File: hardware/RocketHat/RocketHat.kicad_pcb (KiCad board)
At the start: 4 copper layers, 28 x 25 mm, 31 parts, among them J1 Conn_02x16_Top_Bottom, J2 Conn_02x16_Top_Bottom, Q2 MMBT2222A, SW1 SW_DIP_x01, U1 BMP390, U2 BMI088, U3 ADXL375BCCZ, U5 74HC688, U6 74HC245, U7 74HC245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

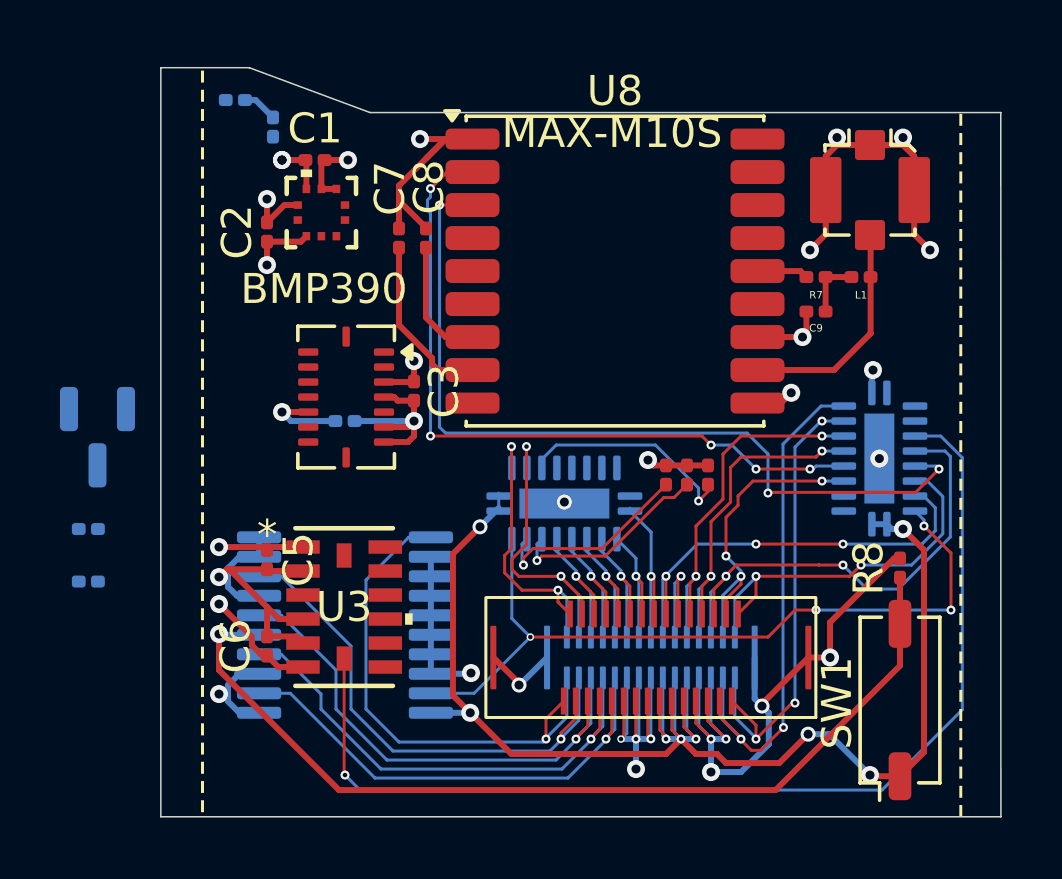
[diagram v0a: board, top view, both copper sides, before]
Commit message: rocket hat finished routing 4 layer
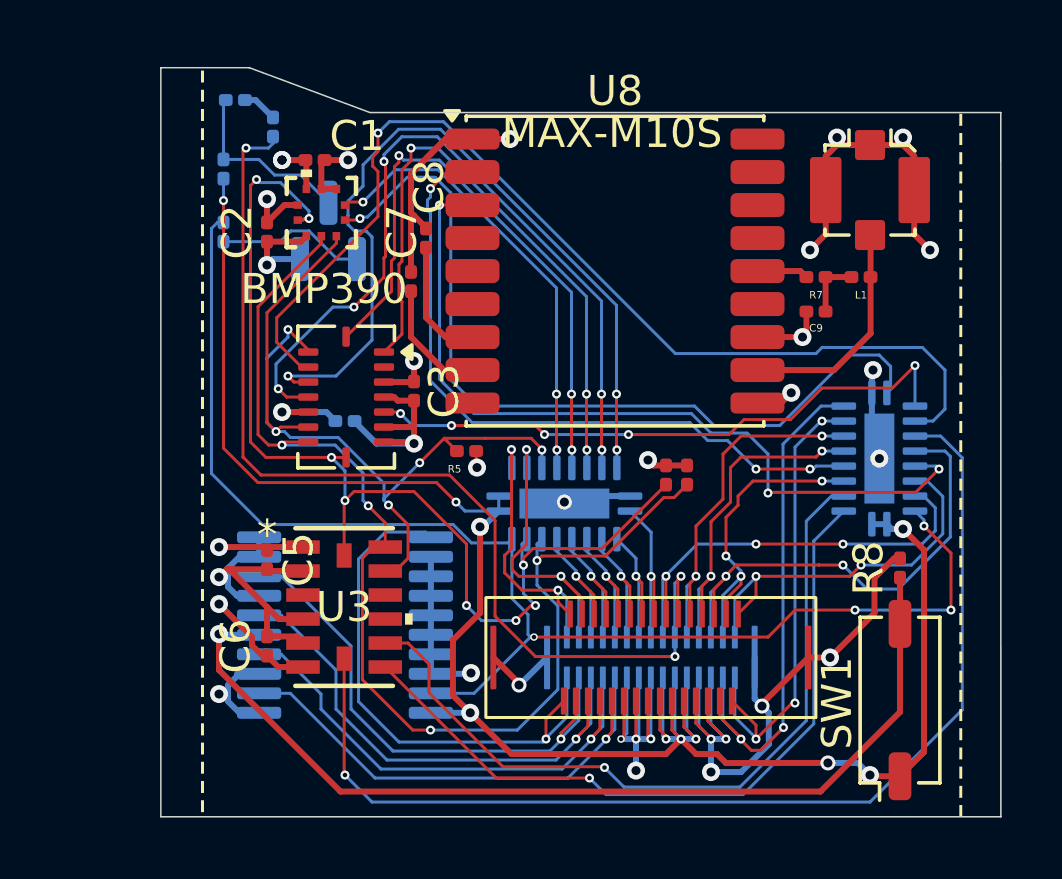
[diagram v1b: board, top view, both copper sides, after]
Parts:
- moved R2 14.5 mm to (130.4, 98.3), turned to -90 degrees
- moved R1 10.9 mm to (130.4, 100.4), turned to -90 degrees
- moved Q2 10.3 mm to (133.9, 100.4), turned to 90 degrees
- moved R5 8.09 mm to (138.6, 107.7), turned to 0 degrees
- moved C7 1.50 mm to (136.7, 102.0)
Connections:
- U7 pad 21: (no net) -> CONN_26/GND
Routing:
- net D13/ACCEL_LOW: track 0.00 -> 35.0 mm, vias 0 -> 1
- net D1/SDI: track 6.83 -> 39.4 mm, vias 1 -> 4
- net CONN_9/RESP: track 3.38 -> 34.6 mm, vias 1 -> 3
- net D0/SCL: track 6.95 -> 36.7 mm, vias 1 -> 8
- net D15/ALTIMETER: track 0.00 -> 27.9 mm, vias 0 -> 1
- net D7/GYRO_INT_2: track 0.00 -> 27.5 mm, vias 0 -> 3
- net D6/GYRO_INT_1: track 0.00 -> 26.2 mm, vias 0 -> 5
- net D9/ACCEL_HIGH_INT_2: track 0.00 -> 25.7 mm, vias 0 -> 1
- net D8/ACCEL_HIGH_INT_1: track 0.00 -> 24.5 mm, vias 0 -> 1
- net D2/SDO: track 7.41 -> 29.6 mm, vias 1 -> 5
- net D5/ACCEL_LOW_INT_2: track 0.00 -> 20.9 mm, vias 0 -> 3
- net D14/GYRO: track 0.00 -> 20.4 mm, vias 0 -> 5
- net D4/ACCEL_LOW_INT_1: track 0.00 -> 20.3 mm, vias 0 -> 3
- net Net-(U5-P=R): track 26.0 -> 45.6 mm
- net CONN_23/5V: track 47.6 -> 65.6 mm, vias 8 -> 10
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
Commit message: rocket hat done
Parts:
- removed SW1: SW_DIP_x01, Button_Switch_SMD:SW_DIP_SPSTx01_Slide_Copal_CHS-01A_W5.08mm_P1.27mm_JPin
- added TP1: TestPoint, TestPoint:TestPoint_Pad_1.5x1.5mm, F.Cu at (153.6, 115.4)
- added TP2: TestPoint, TestPoint:TestPoint_Pad_1.5x1.5mm, F.Cu at (153.6, 117.9)
- moved R8 1.80 mm to (153.0, 113.4)
- moved C9 0.40 mm to (150.2, 102.7)
- moved C5 0.36 mm to (131.6, 111.2)
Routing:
- net CONN_20/3V3: track 37.3 -> 39.5 mm, vias 13 -> 14
- net Net-(U5-R1): track 32.5 -> 31.2 mm
- net CONN_23/5V: track 65.6 -> 66.8 mm
- net CONN_26/GND: track 87.7 -> 87.4 mm, vias 22 -> 23
- net CONN_29/D14: vias 3 -> 2
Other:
- board text added: "Alt ID"
